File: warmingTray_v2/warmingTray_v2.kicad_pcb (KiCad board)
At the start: 2 copper layers, 13 parts, among them J1 Jack-DC, P1 Power, P2 Analog, P3 Analog, P4 Digital, P5 PWM, P6 PWM, P7 Communication

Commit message: PCB update
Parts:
- added 8VReg1: LM78M05_TO252, Package_TO_SOT_SMD:TO-252-2, F.Cu at (133.6, 112.2)
- added BO1: Conn_01x06, Connector_PinHeader_2.54mm:PinHeader_1x06_P2.54mm_Vertical, F.Cu at (111.8, 78.7)
- added BO2: Conn_01x06, Connector_PinHeader_2.54mm:PinHeader_1x06_P2.54mm_Vertical, F.Cu at (132.1, 78.7)
- added BO3: Conn_01x06, Connector_PinHeader_2.54mm:PinHeader_1x06_P2.54mm_Vertical, F.Cu at (152.4, 78.7)
- added BO4: Conn_01x06, Connector_PinHeader_2.54mm:PinHeader_1x06_P2.54mm_Vertical, F.Cu at (172.7, 78.7)
- added BO5: Conn_01x06, Connector_PinHeader_2.54mm:PinHeader_1x06_P2.54mm_Vertical, F.Cu at (111.8, 86.4)
- added BO6: Conn_01x06, Connector_PinHeader_2.54mm:PinHeader_1x06_P2.54mm_Vertical, F.Cu at (132.1, 86.4)
- added BO7: Conn_01x06, Connector_PinHeader_2.54mm:PinHeader_1x06_P2.54mm_Vertical, F.Cu at (152.4, 86.4)
- added BO8: Conn_01x06, Connector_PinHeader_2.54mm:PinHeader_1x06_P2.54mm_Vertical, F.Cu at (172.7, 86.4)
- moved PAD1-1 81.2 mm to (182.9, 96.5), turned to 0 degrees
- moved PAD5-1 69.1 mm to (172.7, 96.5), turned to 0 degrees
- moved LED1 51.1 mm to (198.1, 114.3), turned to 180 degrees
- moved LCDR1 37.8 mm to (193.0, 78.7)
- moved P5 33.1 mm to (133.1, 71.1)
- moved P6 28.5 mm to (160.0, 71.1)
- moved P7 25.0 mm to (182.9, 71.1)
- moved J1 21.8 mm to (113.7, 114.3), turned to -90 degrees
- moved P4 18.3 mm to (208.3, 71.1)
- moved P1 12.5 mm to (142.2, 119.1)
- moved P2 10.8 mm to (165.1, 119.4)
- moved P3 10.8 mm to (188.0, 119.4)
- moved 5VReg1 4.27 mm to (123.4, 112.2)
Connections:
- LED1 pad 13: /30 -> /32
- LED1 pad 14: /32 -> /34
- P1 pad 3: unconnected-(P1-Pad3) -> /RESET
- P4 pad 1: Net-(P4-Pad1) -> GND
- P4 pad 2: Net-(P4-Pad1) -> GND
- P4 pad 35: unconnected-(P4-Pad35) -> +5V
- P4 pad 36: unconnected-(P4-Pad36) -> +5V
- P4 pad 5: unconnected-(P4-Pad5) -> /50
- PAD1-1 pad 2: /Pad2 -> +12V
- PAD1-1 pad 3: /Pad3 -> /Pad2
- PAD1-1 pad 4: /Pad4 -> +12V
- PAD1-1 pad 5: +12V -> /Pad3
- PAD1-1 pad 7: +12V -> /Pad4
- PAD5-1 pad 2: /Pad6 -> +12V
- PAD5-1 pad 3: /Pad7 -> /Pad6
- PAD5-1 pad 4: /Pad8 -> +12V
- PAD5-1 pad 5: +12V -> /Pad7
- PAD5-1 pad 7: +12V -> /Pad8
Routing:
- net GND: vias 0 -> 1
- added copper zone on B.Cu, net GND
- added copper zone on F.Cu, net GND

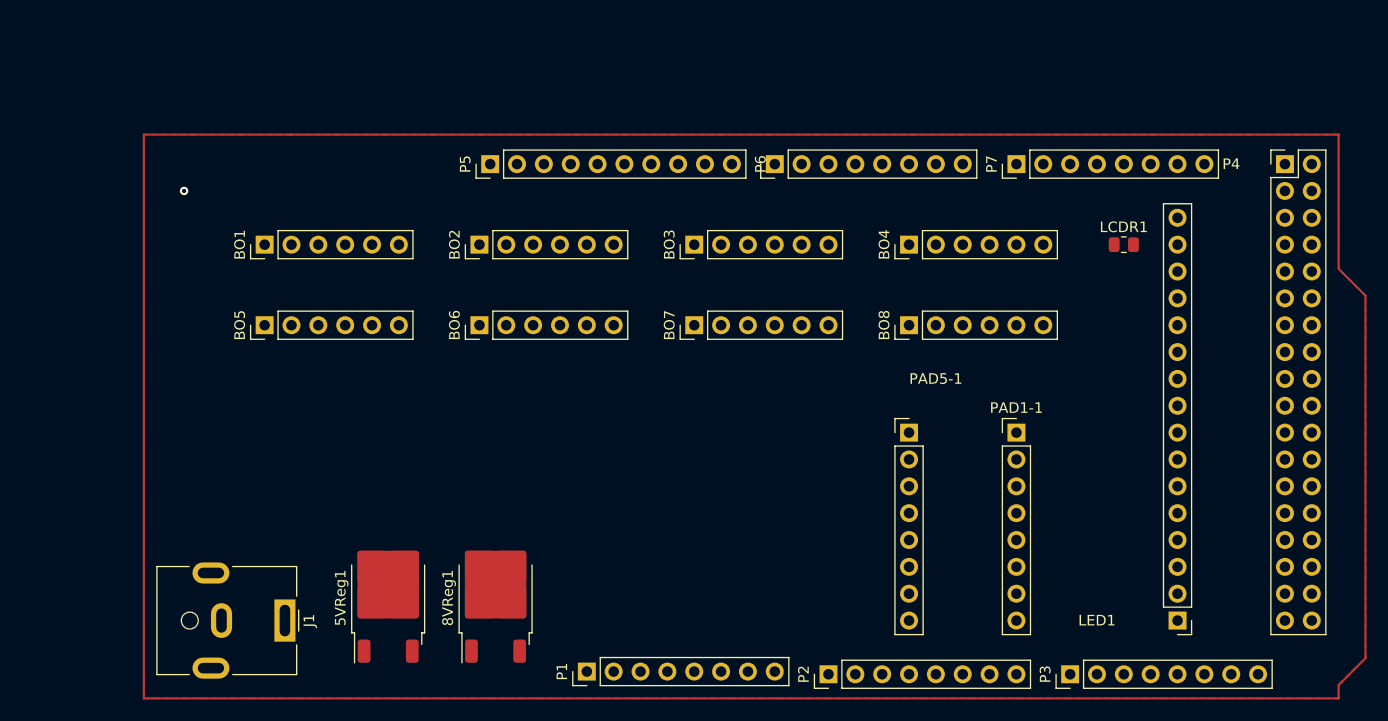
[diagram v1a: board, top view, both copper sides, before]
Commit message: PCB Update: added transistors and pinouts
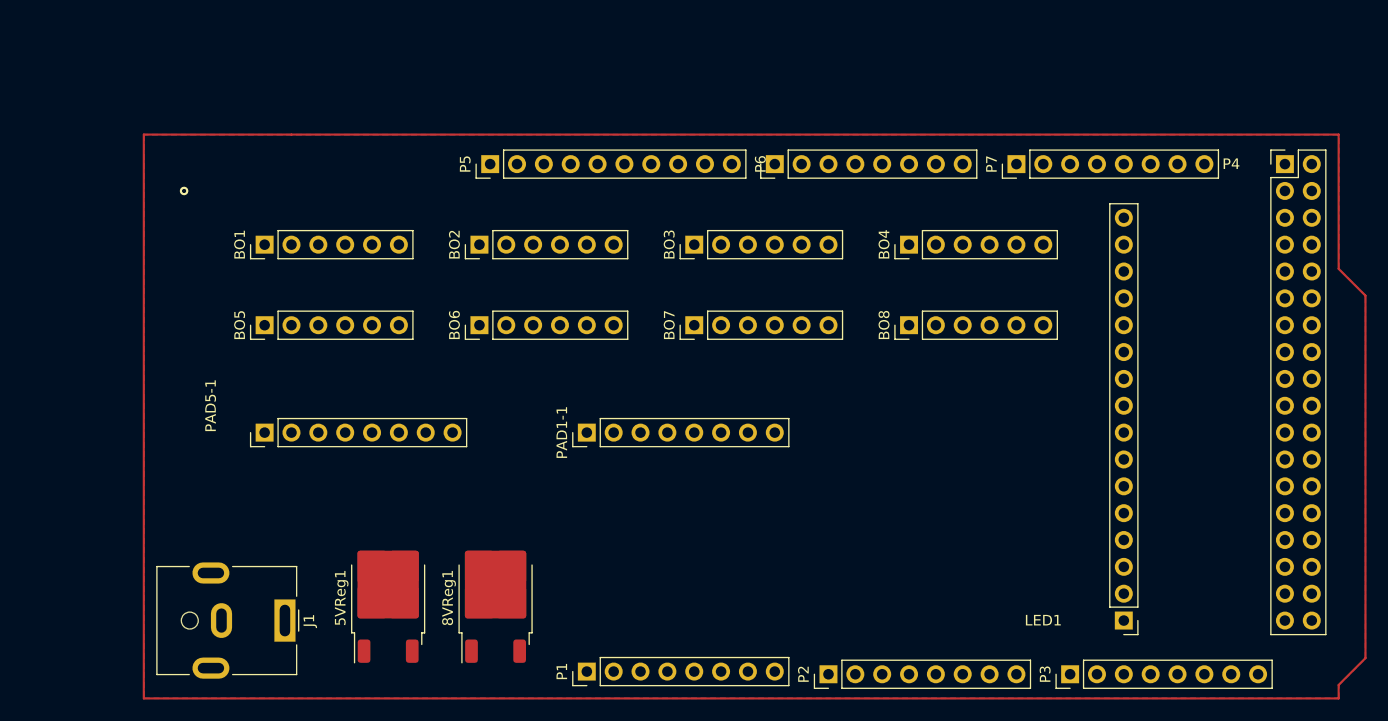
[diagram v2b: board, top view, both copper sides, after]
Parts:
- removed LCDR1: 220, Resistor_SMD:R_0805_2012Metric
- moved PAD5-1 61.0 mm to (111.8, 96.5), turned to 90 degrees
- moved PAD1-1 40.6 mm to (142.2, 96.5), turned to 90 degrees
- moved LED1 5.08 mm to (193.0, 114.3)
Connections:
- BO1 pad 2: unconnected-(BO1-Pin_2-Pad2) -> GND
- BO1 pad 3: unconnected-(BO1-Pin_3-Pad3) -> /13(**)
- BO1 pad 4: unconnected-(BO1-Pin_4-Pad4) -> /12(**)
- BO1 pad 5: unconnected-(BO1-Pin_5-Pad5) -> /11(**)
- BO1 pad 6: unconnected-(BO1-Pin_6-Pad6) -> /10(**)
- BO2 pad 2: unconnected-(BO2-Pin_2-Pad2) -> GND
- BO2 pad 3: unconnected-(BO2-Pin_3-Pad3) -> /13(**)
- BO2 pad 4: unconnected-(BO2-Pin_4-Pad4) -> /12(**)
- BO2 pad 5: unconnected-(BO2-Pin_5-Pad5) -> /11(**)
- BO2 pad 6: unconnected-(BO2-Pin_6-Pad6) -> /9(**)
- BO3 pad 2: unconnected-(BO3-Pin_2-Pad2) -> GND
- BO3 pad 3: unconnected-(BO3-Pin_3-Pad3) -> /13(**)
- BO3 pad 4: unconnected-(BO3-Pin_4-Pad4) -> /12(**)
- BO3 pad 5: unconnected-(BO3-Pin_5-Pad5) -> /11(**)
- BO3 pad 6: unconnected-(BO3-Pin_6-Pad6) -> /8(**)
- BO4 pad 2: unconnected-(BO4-Pin_2-Pad2) -> GND
- BO4 pad 3: unconnected-(BO4-Pin_3-Pad3) -> /13(**)
- BO4 pad 4: unconnected-(BO4-Pin_4-Pad4) -> /12(**)
- BO4 pad 5: unconnected-(BO4-Pin_5-Pad5) -> /11(**)
- BO4 pad 6: unconnected-(BO4-Pin_6-Pad6) -> /7(**)
- BO5 pad 2: unconnected-(BO5-Pin_2-Pad2) -> GND
- BO5 pad 3: unconnected-(BO5-Pin_3-Pad3) -> /13(**)
- BO5 pad 4: unconnected-(BO5-Pin_4-Pad4) -> /12(**)
- BO5 pad 5: unconnected-(BO5-Pin_5-Pad5) -> /11(**)
- BO5 pad 6: unconnected-(BO5-Pin_6-Pad6) -> /6(**)
- BO6 pad 2: unconnected-(BO6-Pin_2-Pad2) -> GND
- BO6 pad 3: unconnected-(BO6-Pin_3-Pad3) -> /13(**)
- BO6 pad 4: unconnected-(BO6-Pin_4-Pad4) -> /12(**)
- BO6 pad 5: unconnected-(BO6-Pin_5-Pad5) -> /11(**)
- BO6 pad 6: unconnected-(BO6-Pin_6-Pad6) -> /5(**)
- BO7 pad 2: unconnected-(BO7-Pin_2-Pad2) -> GND
- BO7 pad 3: unconnected-(BO7-Pin_3-Pad3) -> /13(**)
- BO7 pad 4: unconnected-(BO7-Pin_4-Pad4) -> /12(**)
- BO7 pad 5: unconnected-(BO7-Pin_5-Pad5) -> /11(**)
- BO7 pad 6: unconnected-(BO7-Pin_6-Pad6) -> /4(**)
- BO8 pad 2: unconnected-(BO8-Pin_2-Pad2) -> GND
- BO8 pad 3: unconnected-(BO8-Pin_3-Pad3) -> /13(**)
- BO8 pad 4: unconnected-(BO8-Pin_4-Pad4) -> /12(**)
- BO8 pad 5: unconnected-(BO8-Pin_5-Pad5) -> /11(**)
- BO8 pad 6: unconnected-(BO8-Pin_6-Pad6) -> /3(**)
- LED1 pad 11: /26 -> /28
- LED1 pad 12: /28 -> /30
- LED1 pad 15: /Anode -> /VCC5
- LED1 pad 3: /10(**) -> /22
- LED1 pad 4: /22 -> /24
- LED1 pad 6: /24 -> /26

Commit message: small changes
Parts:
- moved LED1 5.08 mm to (198.1, 114.3)
- moved 8VReg1 3.25 mm to (135.6, 109.6)
- moved 5VReg1 2.54 mm to (123.4, 109.6)
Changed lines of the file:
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@@
   )
   (footprint "Package_TO_SOT_SMD:TO-252-2" (layer "F.Cu")
-    (at 123.445 112.155 90)
+    (at 123.445 109.615 90)
     (descr "TO-252/DPAK SMD package, http://www.infineon.com/cms/en/product/packages/PG-TO252/PG-TO252-3-1/")
     (tags "DPAK TO-252 DPAK-3 TO-252-3 SOT-428")
@@
   )
   (footprint "Package_TO_SOT_SMD:TO-252-2" (layer "F.Cu")
-    (at 133.605 112.155 90)
+    (at 135.635 109.615 90)
     (descr "TO-252/DPAK SMD package, http://www.infineon.com/cms/en/product/packages/PG-TO252/PG-TO252-3-1/")
     (tags "DPAK TO-252 DPAK-3 TO-252-3 SOT-428")
@@
   )
   (footprint "Connector_PinHeader_2.54mm:PinHeader_1x16_P2.54mm_Vertical" (layer "F.Cu")
-    (at 193.04 114.3 180)
+    (at 198.12 114.3 180)
     (descr "Through hole straight pin header, 1x16, 2.54mm pitch, single row")
     (tags "Through hole pin header THT 1x16 2.54mm single row")
